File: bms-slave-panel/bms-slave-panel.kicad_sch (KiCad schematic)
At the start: 62 parts, among them J1 Conn_02x10_Odd_Even, J2 Conn_02x10_Odd_Even, J3 Conn_02x10_Odd_Even, J4 Conn_02x10_Odd_Even

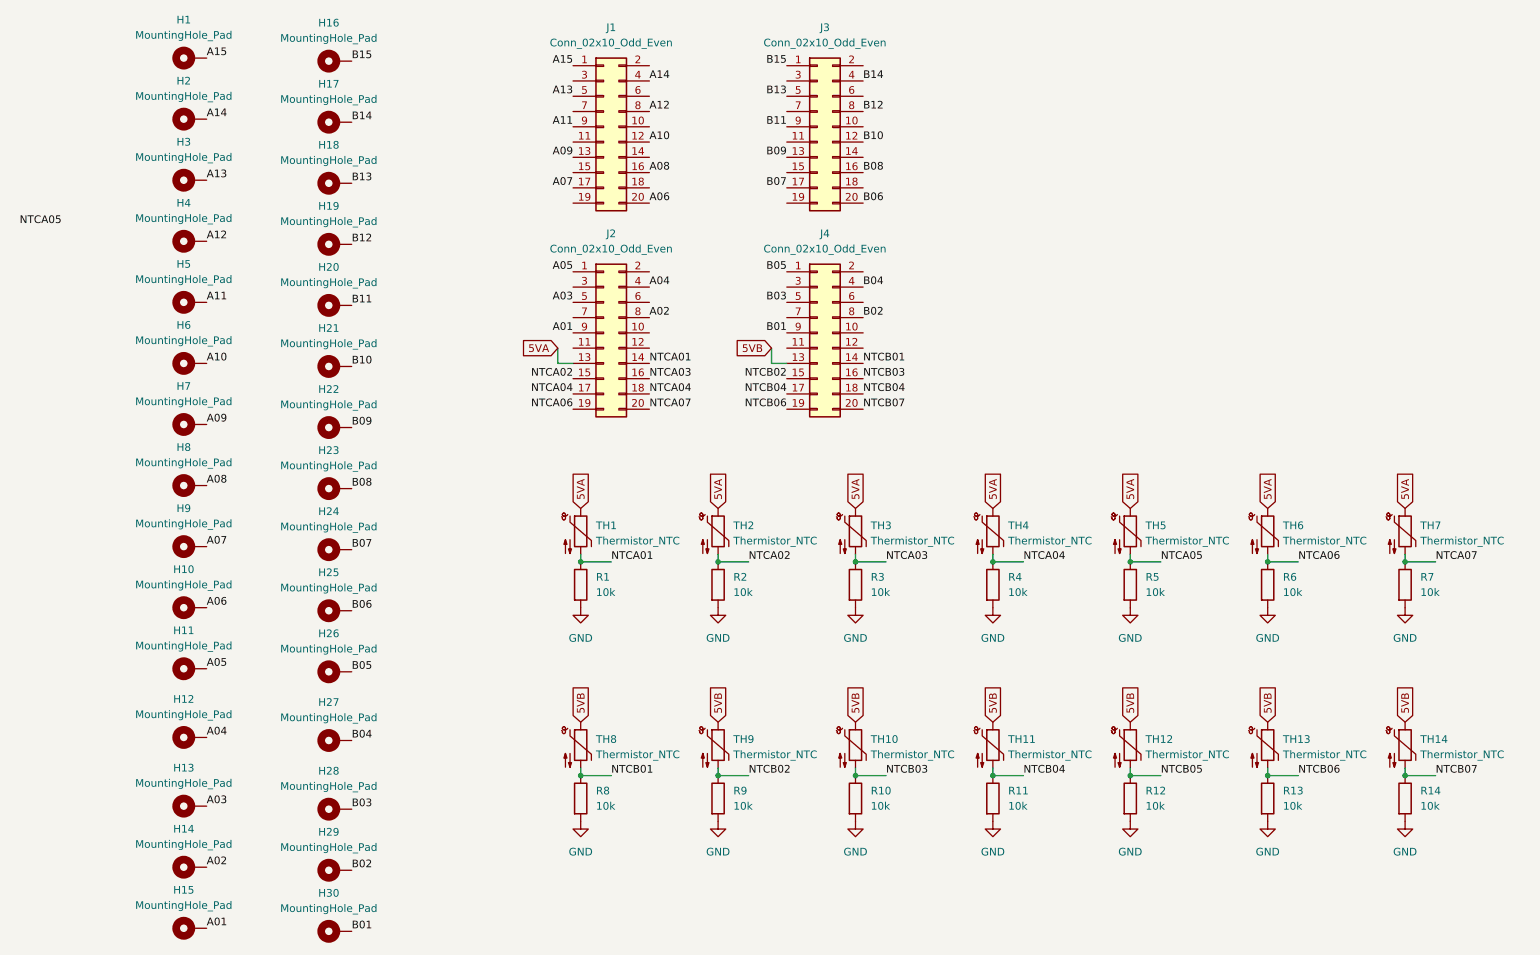
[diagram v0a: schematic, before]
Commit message: feat: complete bms panel layout
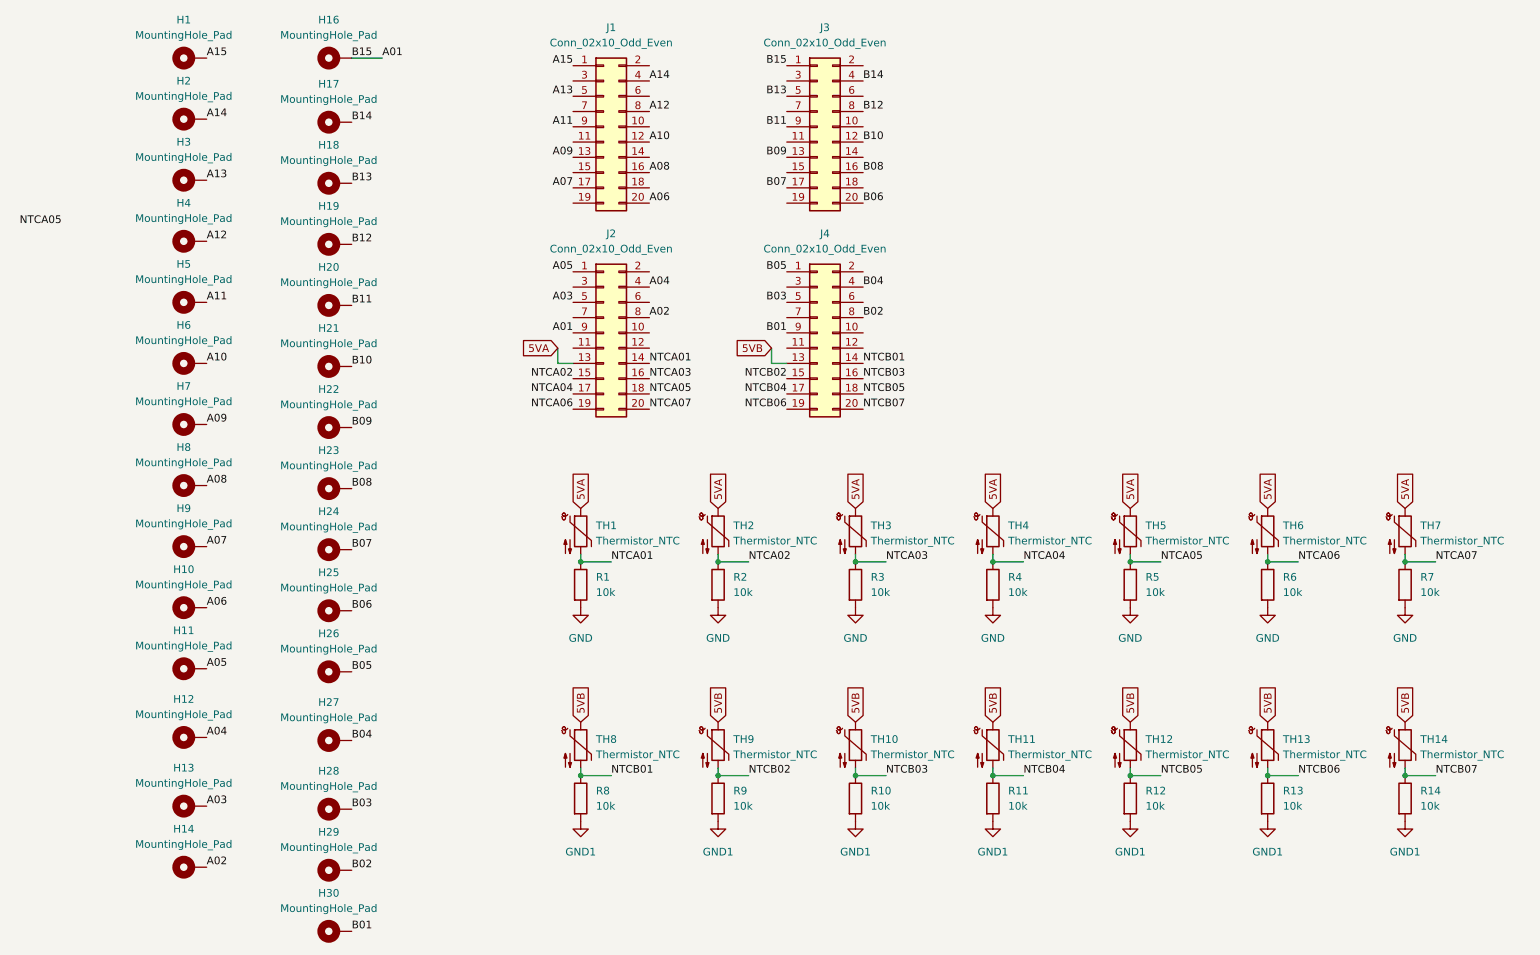
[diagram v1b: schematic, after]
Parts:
- removed H15: MountingHole_Pad, MountingHole:MountingHole_4.3mm_M4_DIN965_Pad, symbol Mechanical:MountingHole_Pad
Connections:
- net B15 is gone; now on net A01: H16.1, J3.1 (Pin_1)
- net GND: no longer R10.2, R11.2, R12.2, R13.2, R14.2, R8.2, R9.2
- net NTCA04: no longer J2.18 (Pin_18)
- net NTCA05: now also J2.18 (Pin_18)
- net NTCB04: no longer J4.18 (Pin_18)
- net NTCB05: now also J4.18 (Pin_18)
- new net GND1: R10.2, R11.2, R12.2, R13.2, R14.2, R8.2, R9.2
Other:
- moved on the sheet: H16

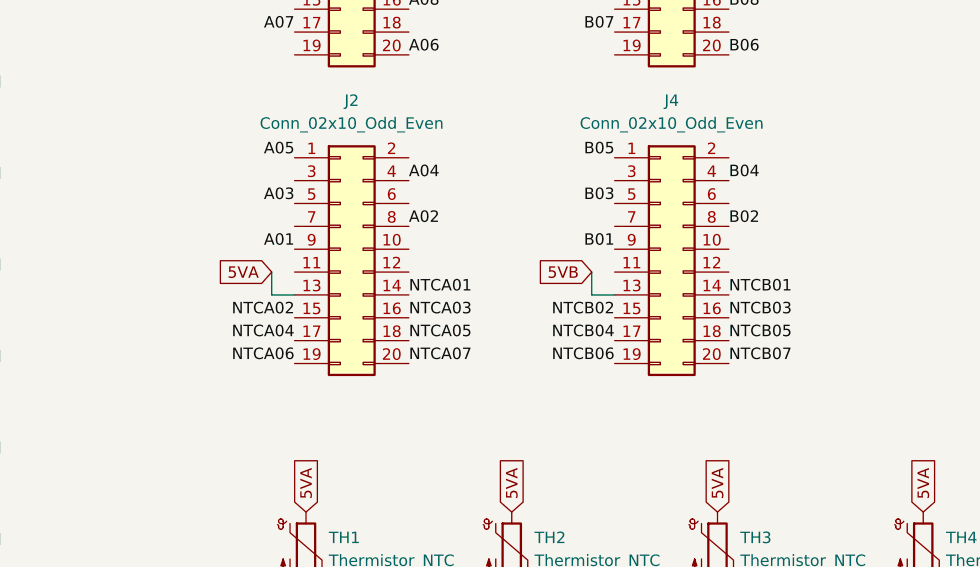
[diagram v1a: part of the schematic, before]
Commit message: fix: panel channel A0 & B15
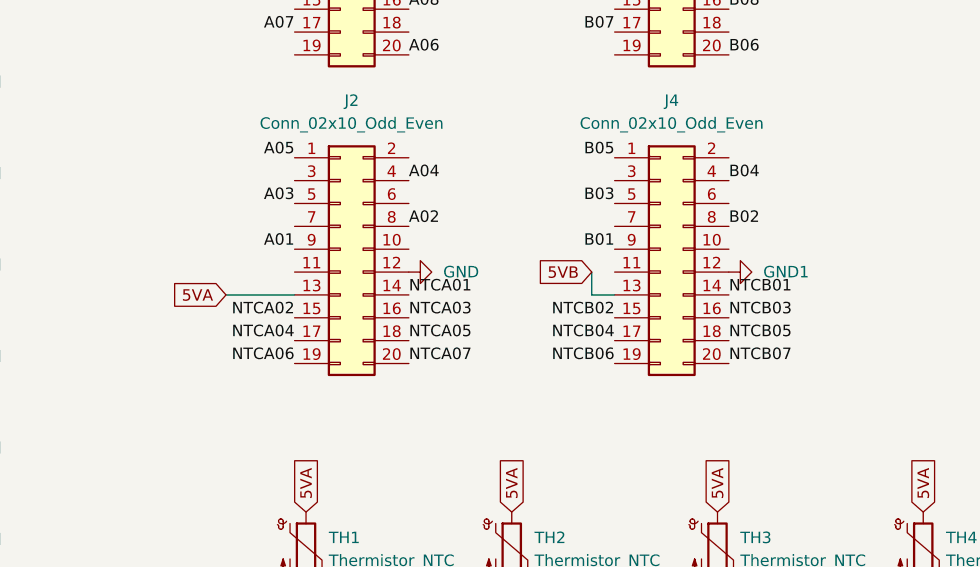
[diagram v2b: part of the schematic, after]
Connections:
- net GND: now also J2.12 (Pin_12)
- net GND1: now also J4.12 (Pin_12)
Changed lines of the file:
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@@
 	(wire
 		(pts
-			(xy 96.52 77.47) (xy 96.52 80.01)
-		)
-		(stroke
-			(width 0)
-			(type default)
-		)
-	)
-	(wire
-		(pts
 			(xy 237.49 111.76) (xy 237.49 113.03)
 		)
@@
 	(wire
 		(pts
-			(xy 96.52 80.01) (xy 99.06 80.01)
+			(xy 91.44 80.01) (xy 99.06 80.01)
 		)
 		(stroke
@@
 	(global_label "5VA"
 		(shape input)
-		(at 96.52 77.47 180)
+		(at 91.44 80.01 180)
 		(fields_autoplaced yes)
 		(effects
@@
 		)
 		(property "Intersheetrefs" "${INTERSHEET_REFS}"
-			(at 90.1481 77.47 0)
+			(at 85.0681 80.01 0)
 			(effects
 				(font
@@
 	)
 	(symbol
+		(lib_id "power:GND")
+		(at 111.76 77.47 90)
+		(unit 1)
+		(exclude_from_sim no)
+		(in_bom yes)
+		(on_board yes)
+		(dnp no)
+		(fields_autoplaced yes)
+		(property "Reference" "#PWR15"
+			(at 118.11 77.47 0)
+			(effects
+				(font
+					(size 1.27 1.27)
+				)
+				(hide yes)
+			)
+		)
+		(property "Value" "GND"
+			(at 115.57 77.4699 90)
+			(effects
+				(font
+					(size 1.27 1.27)
+				)
+				(justify right)
+			)
+		)
+		(property "Footprint" ""
+			(at 111.76 77.47 0)
+			(effects
+				(font
+					(size 1.27 1.27)
+				)
+				(hide yes)
+			)
+		)
+		(property "Datasheet" ""
+			(at 111.76 77.47 0)
+			(effects
+				(font
+					(size 1.27 1.27)
+				)
+				(hide yes)
+			)
+		)
+		(property "Description" "Power symbol creates a global label with name \"GND\" , ground"
+			(at 111.76 77.47 0)
+			(effects
+				(font
+					(size 1.27 1.27)
+				)
+				(hide yes)
+			)
+		)
+		(pin "1"
+		)
+		(instances
+			(project "bms-slave-panel"
+				(path "/3e9613e6-0d78-4568-887e-2649ee969256"
+					(reference "#PWR15")
+					(unit 1)
+				)
+			)
+		)
+	)
+	(symbol
 		(lib_id "Device:Thermistor_NTC")
 		(at 146.05 107.95 0)
@@
 					(unit 1)
 				)
+			)
+		)
+	)
+	(symbol
+		(lib_id "power:GND1")
+		(at 147.32 77.47 90)
+		(unit 1)
+		(exclude_from_sim no)
+		(in_bom yes)
+		(on_board yes)
+		(dnp no)
+		(fields_autoplaced yes)
+		(property "Reference" "#PWR16"
+			(at 153.67 77.47 0)
+			(effects
+				(font
+					(size 1.27 1.27)
+				)
+				(hide yes)
+			)
+		)
+		(property "Value" "GND1"
+			(at 151.13 77.4699 90)
+			(effects
+				(font
+					(size 1.27 1.27)
+				)
+				(justify right)
+			)
+		)
+		(property "Footprint" ""
+			(at 147.32 77.47 0)
+			(effects
+				(font
+					(size 1.27 1.27)
+				)
+				(hide yes)
+			)
+		)
+		(property "Datasheet" ""
+			(at 147.32 77.47 0)
+			(effects
+				(font
+					(size 1.27 1.27)
+				)
+				(hide yes)
+			)
+		)
+		(property "Description" "Power symbol creates a global label with name \"GND1\" , ground"
+			(at 147.32 77.47 0)
+			(effects
+				(font
+					(size 1.27 1.27)
+				)
+				(hide yes)
+			)
+		)
+		(pin "1"
+		)
+		(instances
+			(project "bms-slave-panel"
+				(path "/3e9613e6-0d78-4568-887e-2649ee969256"
+					(reference "#PWR16")
+					(unit 1)
+				)
